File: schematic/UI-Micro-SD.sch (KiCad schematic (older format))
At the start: 31 parts, among them IC1 TCA9534PWR, J1 Conn_02x08_Odd_Even, J2 Conn_02x08_Odd_Even, J6 Conn_01x08, J8 Solder-Jumper-3-3-3-Open, Q1 BSS138, U1 SFV14R-2STE1HLF, U2 DizzyBITLogo, U3 DizzyBIT-Layout

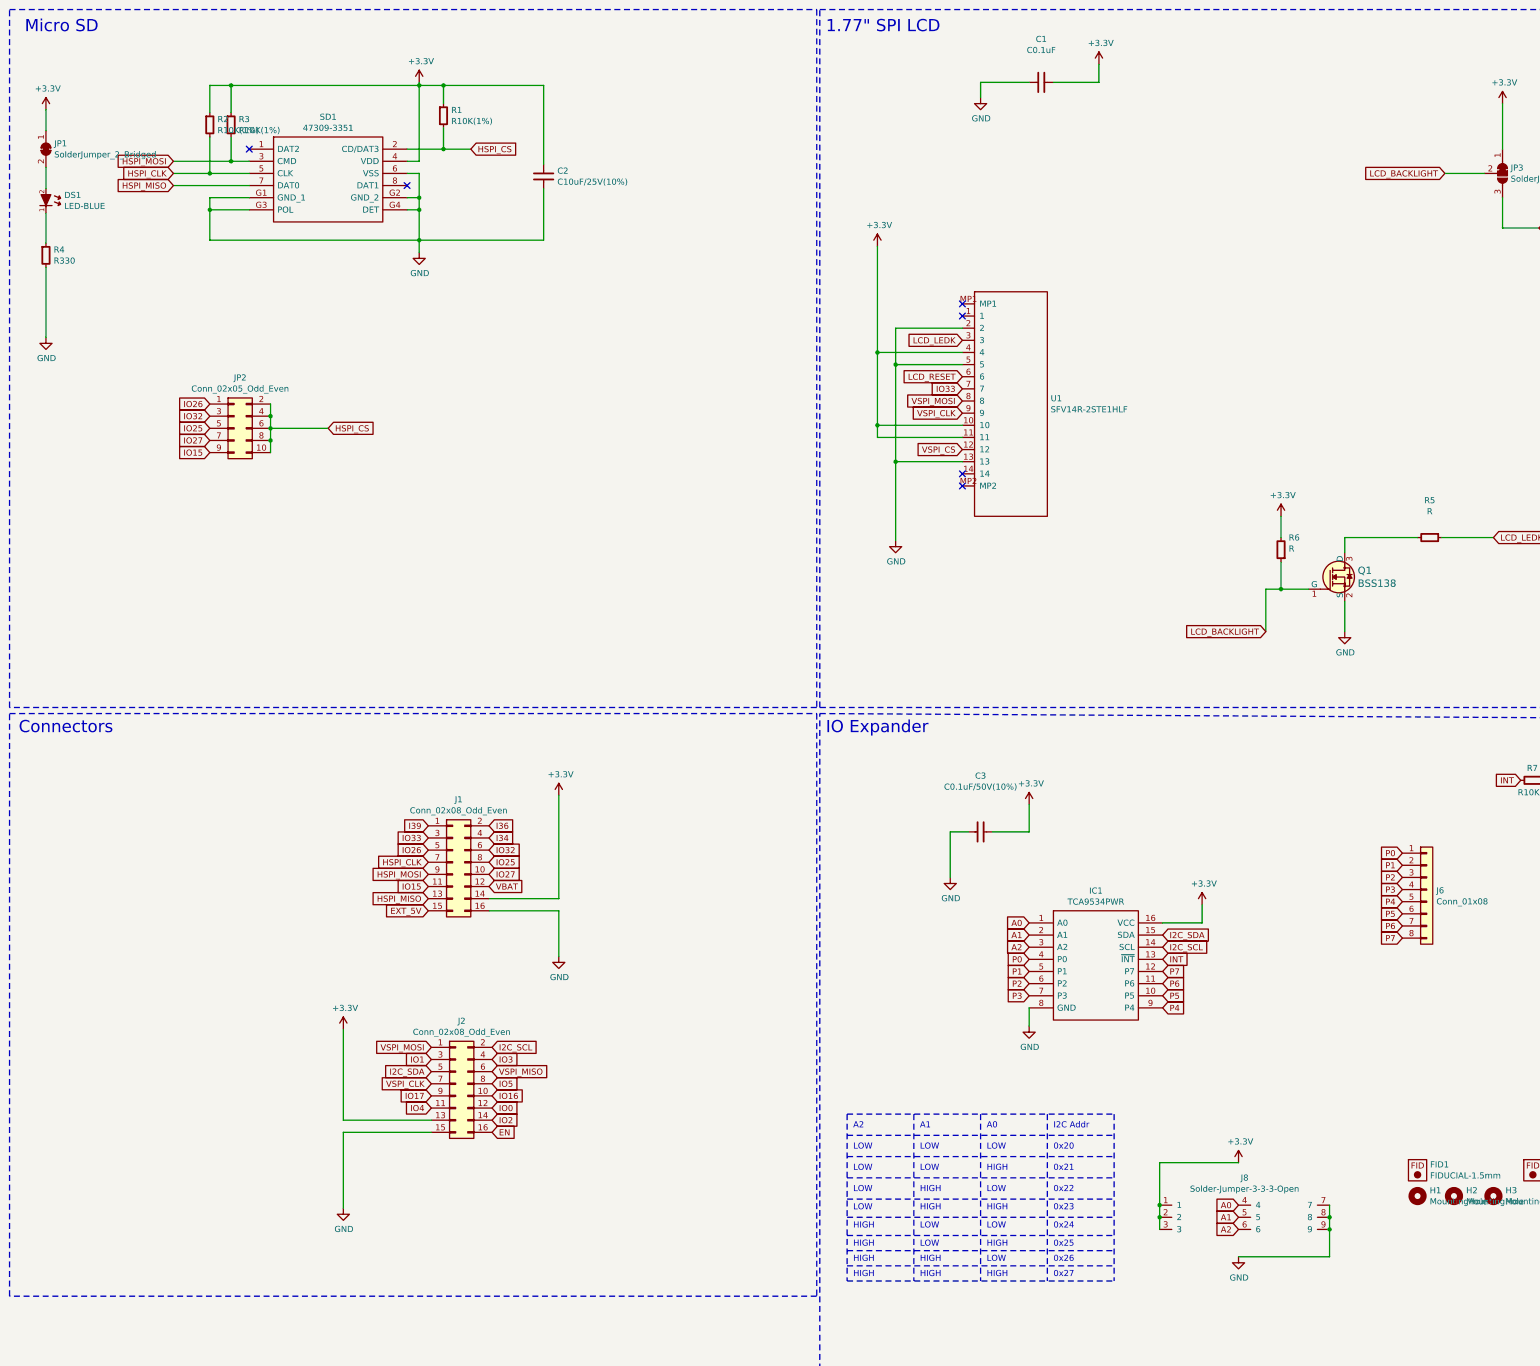
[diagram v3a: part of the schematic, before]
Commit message: Fixed PN-s for display connector and IO expander
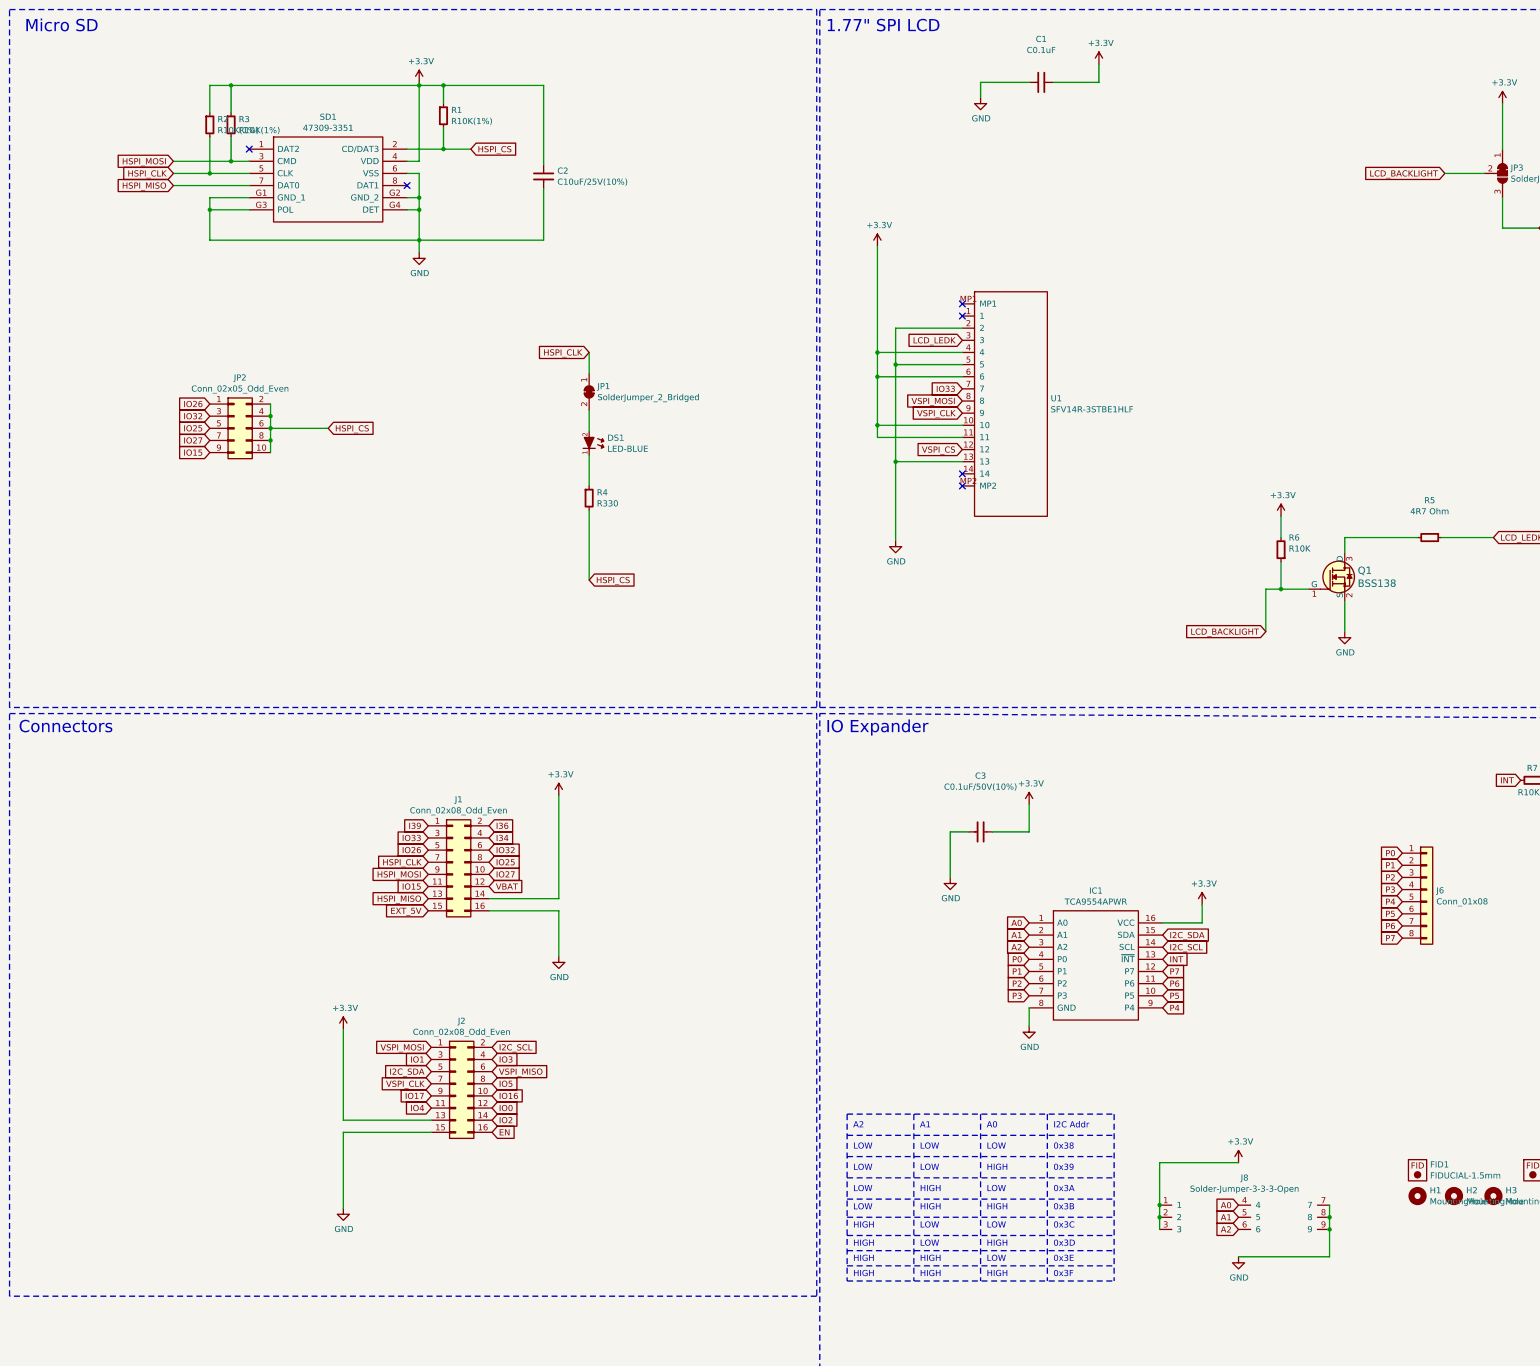
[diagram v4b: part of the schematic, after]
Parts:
- removed IC1: TCA9534PWR, undo:SOP65P640X120-16N, symbol SamacSys_Parts:TCA9534PWR
- added IC1: TCA9554APWR, SOP65P640X120-16N, symbol SamacSys_Parts:TCA9554APWR
- R5: value R -> 4R7 Ohm; pn (none) -> RC0603JR-074R7L
- R6: value R -> R10K; pn ESR03EZPJ103 -> ESR03EZPJ103
- SD1: Description Molex 47309 Series 8 Way Right Angle Micro SD Memory Card C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 -> (none); Height 3.35 -> (none); Manufacturer_Name Molex -> Connfly; Manufacturer_Part_Number 47309-3351 -> DS1139-05; Mouser Part Number 538-47309-3351 -> (none); dk_pn WM10795DKR-ND -> (none); pn 47309-3351 -> DS1139-05
- U1: value SFV14R-2STE1HLF -> SFV14R-3STBE1HLF; footprint undo:SFV14R-2STE1HLF -> undo:SFV14R-3STBE1HLF
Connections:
- net LCD_RESET is gone; now on net +3V3: U1.6
- net +3V3: now also IC1.16 (VCC); no longer JP1.1 (A)
- net A0: now also IC1.1 (A0)
- net A1: now also IC1.2 (A1)
- net A2: now also IC1.3 (A2)
- net GND: now also IC1.8 (GND); no longer R4.2
- net HSPI_CLK: now also JP1.1 (A)
- net HSPI_CS: now also R4.2
- net I2C_SCL: now also IC1.14 (SCL)
- net I2C_SDA: now also IC1.15 (SDA)
- net INT: now also IC1.13 (~INT)
- net P0: now also IC1.4 (P0)
- net P1: now also IC1.5 (P1)
- net P2: now also IC1.6 (P2)
- net P3: now also IC1.7 (P3)
- net P4: now also IC1.9 (P4)
- net P5: now also IC1.10 (P5)
- net P6: now also IC1.11 (P6)
- net P7: now also IC1.12 (P7)
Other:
- note added: "0x38"
- note added: "0x39"
- note added: "0x3A"
- note added: "0x3B"
- note added: "0x3C"
- note added: "0x3D"
- note added: "0x3E"
- note added: "0x3F\n"
- note removed: "0x20"
- note removed: "0x21"
- note removed: "0x22"
- note removed: "0x23"
- note removed: "0x24"
- note removed: "0x25"
- note removed: "0x26"
- note removed: "0x27\n"
- moved on the sheet: DS1, JP1, R4
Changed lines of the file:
@@
 L _semi:LED DS1
 U 1 1 5C6120FB
-P 875 2150
-F 0 "DS1" H 1025 2196 50  0000 L CNN
-F 1 "LED-BLUE" H 1025 2105 50  0000 L CNN
-F 2 "LED_SMD:LED_0805_2012Metric" H 1025 2104 60  0001 L CNN
-F 3 "" H 875 2150 60  0001 C CNN
-F 4 "160-1579-1-ND" H 1025 2006 50  0001 L CNN "dk_pn"
-F 5 "LTST-C170TBKT" H 875 2150 50  0001 C CNN "pn"
-F 6 "https://www.digikey.com/product-detail/en/lite-on-inc/LTST-C170TBKT/160-1579-1-ND/564889" H 875 2150 50  0001 C CNN "dk_web"
-	1    875  2150
+P 5350 4150
+F 0 "DS1" H 5500 4196 50  0000 L CNN
+F 1 "LED-BLUE" H 5500 4105 50  0000 L CNN
+F 2 "LED_SMD:LED_0805_2012Metric" H 5500 4104 60  0001 L CNN
+F 3 "" H 5350 4150 60  0001 C CNN
+F 4 "160-1579-1-ND" H 5500 4006 50  0001 L CNN "dk_pn"
+F 5 "LTST-C170TBKT" H 5350 4150 50  0001 C CNN "pn"
+F 6 "https://www.digikey.com/product-detail/en/lite-on-inc/LTST-C170TBKT/160-1579-1-ND/564889" H 5350 4150 50  0001 C CNN "dk_web"
+	1    5350 4150
 	1    0    0    -1
 $EndComp
@@
 L _passive:R R4
 U 1 1 5C61218D
-P 875 2600
-F 0 "R4" H 938 2646 50  0000 L CNN
-F 1 "R330" H 938 2555 50  0000 L CNN
-F 2 "Resistor_SMD:R_0603_1608Metric" H 875 2650 60  0001 C CNN
-F 3 "" H 875 2650 60  0001 C CNN
-F 4 "CR0603-JW-331ELFCT-ND" H 875 2600 50  0001 C CNN "dk_pn"
-F 5 "CR0603-JW-331ELF" H 875 2600 50  0001 C CNN "pn"
-F 6 "https://www.digikey.com/product-detail/en/bourns-inc/CR0603-JW-331ELF/CR0603-JW-331ELFCT-ND/3767680" H 875 2600 50  0001 C CNN "dk_web"
-	1    875  2600
-	1    0    0    -1
-$EndComp
-$Comp
-L power:+3.3V #PWR0101
-U 1 1 5C6121E5
-P 875 1400
-F 0 "#PWR0101" H 875 1250 50  0001 C CNN
-F 1 "+3.3V" H 890 1573 50  0000 C CNN
-F 2 "" H 875 1400 50  0001 C CNN
-F 3 "" H 875 1400 50  0001 C CNN
-	1    875  1400
-	1    0    0    -1
-$EndComp
-Wire Wire Line
-	875  2050 875  1875
-$Comp
-L power:GND #PWR0102
-U 1 1 5C612F06
-P 875 3275
-F 0 "#PWR0102" H 875 3025 50  0001 C CNN
-F 1 "GND" H 880 3102 50  0000 C CNN
-F 2 "" H 875 3275 50  0001 C CNN
-F 3 "" H 875 3275 50  0001 C CNN
-	1    875  3275
-	1    0    0    -1
-$EndComp
-Wire Wire Line
-	875  2700 875  3275
-Wire Wire Line
-	875  2250 875  2500
+P 5350 4600
+F 0 "R4" H 5413 4646 50  0000 L CNN
+F 1 "R330" H 5413 4555 50  0000 L CNN
+F 2 "Resistor_SMD:R_0603_1608Metric" H 5350 4650 60  0001 C CNN
+F 3 "" H 5350 4650 60  0001 C CNN
+F 4 "CR0603-JW-331ELFCT-ND" H 5350 4600 50  0001 C CNN "dk_pn"
+F 5 "CR0603-JW-331ELF" H 5350 4600 50  0001 C CNN "pn"
+F 6 "https://www.digikey.com/product-detail/en/bourns-inc/CR0603-JW-331ELF/CR0603-JW-331ELFCT-ND/3767680" H 5350 4600 50  0001 C CNN "dk_web"
+	1    5350 4600
+	1    0    0    -1
+$EndComp
+Wire Wire Line
+	5350 4050 5350 3875
+Wire Wire Line
+	5350 4700 5350 5275
+Wire Wire Line
+	5350 4250 5350 4500
 $Comp
 L SamacSys_Parts:47309-3351 SD1
@@
 F 2 "Connfly:DS1139-05" H 3700 1825 50  0001 L CNN
 F 3 "https://componentsearchengine.com/Datasheets/1/47309-3351.pdf" H 3700 1725 50  0001 L CNN
-F 4 "WM10795DKR-ND" H 2550 1725 50  0001 C CNN "dk_pn"
-F 5 "47309-3351" H 2550 1725 50  0001 C CNN "pn"
-F 6 "Molex 47309 Series 8 Way Right Angle Micro SD Memory Card Connector with Solder Termination" H 3700 1625 50  0001 L CNN "Description"
-F 7 "3.35" H 3700 1525 50  0001 L CNN "Height"
-F 8 "538-47309-3351" H 3700 1425 50  0001 L CNN "Mouser Part Number"
-F 9 "Molex" H 3700 1325 50  0001 L CNN "Manufacturer_Name"
-F 10 "47309-3351" H 3700 1225 50  0001 L CNN "Manufacturer_Part_Number"
+F 4 "DS1139-05" H 2550 1725 50  0001 C CNN "pn"
+F 5 "Connfly" H 3700 1325 50  0001 L CNN "Manufacturer_Name"
+F 6 "DS1139-05" H 3700 1225 50  0001 L CNN "Manufacturer_Part_Number"
 	1    2550 1725
 	1    0    0    -1
@@
 P 8525 2850
 F 0 "U1" H 9152 1921 50  0000 L CNN
-F 1 "SFV14R-2STE1HLF" H 9152 1830 50  0000 L CNN
-F 2 "undo:SFV14R-2STE1HLF" H 8525 2850 50  0001 C CNN
+F 1 "SFV14R-3STBE1HLF" H 9152 1830 50  0000 L CNN
+F 2 "undo:SFV14R-3STBE1HLF" H 8525 2850 50  0001 C CNN
 F 3 "" H 8525 2850 50  0001 C CNN
 	1    8525 2850
@@
 Text GLabel 8425 3300 0    50   Input ~ 0
 LCD_LEDK
-Text GLabel 8425 3600 0    50   Input ~ 0
-LCD_RESET
 $Comp
 L OLIMEX_Power:+3.3V #PWR0110
@@
 Connection ~ 7725 3400
 Wire Wire Line
-	7725 3400 7725 4000
+	7725 3400 7725 3600
 $Comp
 L dk_Transistors-FETs-MOSFETs-Single:BSS138 Q1
@@
 P 12275 4925
 F 0 "R5" V 11969 4925 50  0000 C CNN
-F 1 "R" V 12060 4925 50  0000 C CNN
+F 1 "4R7 Ohm" V 12060 4925 50  0000 C CNN
 F 2 "Resistor_SMD:R_0603_1608Metric" V 12159 4925 60  0001 C CNN
 F 3 "" H 12275 4975 60  0000 C CNN
+F 4 "RC0603JR-074R7L " H 12275 4925 50  0001 C CNN "pn"
 	1    12275 4925
 	0    1    1    0
@@
 P 11050 5025
 F 0 "R6" H 10987 4926 50  0000 R CNN
-F 1 "R" H 10987 5017 50  0000 R CNN
+F 1 "R10K" H 10987 5017 50  0000 R CNN
 F 2 "Resistor_SMD:R_0603_1608Metric" H 10987 5116 60  0001 R CNN
 F 3 "" H 11050 5075 60  0000 C CNN
-F 4 "ESR03EZPJ103" H 11050 5025 50  0001 C CNN "pn"
+F 4 "ESR03EZPJ103 " H 11050 5025 50  0001 C CNN "pn"
 	1    11050 5025
 	-1   0    0    1
@@
 Text Notes 7300 775  0    100  ~ 0
 1.77" SPI LCD
-$Comp
-L SamacSys_Parts:TCA9534PWR IC1
-U 1 1 5C5946A2
-P 8975 8100
-F 0 "IC1" H 9525 8365 50  0000 C CNN
-F 1 "TCA9534PWR" H 9525 8274 50  0000 C CNN
-F 2 "undo:SOP65P640X120-16N" H 9925 8200 50  0001 L CNN
-F 3 "http://www.ti.com/lit/ds/symlink/tca9534.pdf" H 9925 8100 50  0001 L CNN
-F 4 "296-40574-1-ND" H 8975 8100 50  0001 C CNN "dk_pn"
-F 5 "TCA9534PWR" H 8975 8100 50  0001 C CNN "pn"
-F 6 "Remote 8-Bit I2C Low-Power I/O Expander With Interrupt Output and Configuration Registers" H 9925 8000 50  0001 L CNN "Description"
-F 7 "1.2" H 9925 7900 50  0001 L CNN "Height"
-F 8 "595-TCA9534PWR" H 9925 7800 50  0001 L CNN "Mouser Part Number"
-F 9 "Texas Instruments" H 9925 7700 50  0001 L CNN "Manufacturer_Name"
-F 10 "TCA9534PWR" H 9925 7600 50  0001 L CNN "Manufacturer_Part_Number"
-	1    8975 8100
-	1    0    0    -1
-$EndComp
 $Comp
 L power:+3.3V #PWR0116
@@
 LOW
 Text Notes 9175 9975 0    50   ~ 0
-0x20
+0x38
 Wire Notes Line
 	7475 10025 9675 10025
@@
 HIGH
 Text Notes 9175 10150 0    50   ~ 0
-0x21
+0x39
 Wire Notes Line
 	7475 10200 9675 10200
@@
 LOW
 Text Notes 9175 10325 0    50   ~ 0
-0x22
+0x3A
 Wire Notes Line
 	7475 10375 9675 10375
@@
 HIGH
 Text Notes 9175 10475 0    50   ~ 0
-0x23
+0x3B
 Wire Notes Line
 	7475 10525 9675 10525
@@
 LOW
 Text Notes 9175 10625 0    50   ~ 0
-0x24
+0x3C
 Wire Notes Line
 	7475 10675 9675 10675
@@
 HIGH
 Text Notes 9175 10775 0    50   ~ 0
-0x25
+0x3D
 Wire Notes Line
 	7475 10800 9675 10800
@@
 LOW
 Text Notes 9175 10900 0    50   ~ 0
-0x26
+0x3E
 Wire Notes Line
 	7475 10925 9675 10925
@@
 HIGH
 Text Notes 9175 11025 0    50   ~ 0
-0x27\n
+0x3F\n
 Wire Notes Line
 	7475 11050 9675 11050
@@
 L Jumper:SolderJumper_2_Bridged JP1
 U 1 1 5D97861B
-P 875 1725
-F 0 "JP1" V 829 1793 50  0000 L CNN
-F 1 "SolderJumper_2_Bridged" V 920 1793 50  0000 L CNN
-F 2 "DizzyBit:DizzyBit-SolderJumper-2-Open" H 875 1725 50  0001 C CNN
-F 3 "~" H 875 1725 50  0001 C CNN
-	1    875  1725
+P 5350 3725
+F 0 "JP1" V 5304 3793 50  0000 L CNN
+F 1 "SolderJumper_2_Bridged" V 5395 3793 50  0000 L CNN
+F 2 "DizzyBit:DizzyBit-SolderJumper-2-Open" H 5350 3725 50  0001 C CNN
+F 3 "~" H 5350 3725 50  0001 C CNN
+	1    5350 3725
 	0    1    1    0
 $EndComp
 Wire Wire Line
-	875  1400 875  1575
+	5350 3400 5350 3575
 NoConn ~ 8425 3000
 Wire Wire Line
@@
 Wire Wire Line
 	10050 10525 10050 10625
+Wire Wire Line
+	8425 3600 7725 3600
+Connection ~ 7725 3600
+Wire Wire Line
+	7725 3600 7725 4000
+Text GLabel 5350 3400 0    50   Input ~ 0
+HSPI_CLK
+Text GLabel 5350 5275 2    50   Input ~ 0
+HSPI_CS
+$Comp
+L SamacSys_Parts:TCA9554APWR IC1
+U 1 1 5DBD5E3F
+P 8975 8100
+F 0 "IC1" H 9525 8365 50  0000 C CNN
+F 1 "TCA9554APWR" H 9525 8274 50  0000 C CNN
+F 2 "SOP65P640X120-16N" H 9925 8200 50  0001 L CNN
+F 3 "http://www.ti.com/lit/gpn/tca9554a" H 9925 8100 50  0001 L CNN
+F 4 "Texas Instruments TCA9554APWR, 8-channel 8bit I/O Expander 400kHz, I2C, SMBus, 16-Pin TSSOP" H 9925 8000 50  0001 L CNN "Description"
+F 5 "" H 9925 7900 50  0001 L CNN "Height"
+F 6 "595-TCA9554APWR" H 9925 7800 50  0001 L CNN "Mouser Part Number"
+F 7 "https://www.mouser.com/Search/ProductDetail.aspx?qs=O1HRStiETCjcEMAC%252bg%252bJsA%3d%3d" H 9925 7700 50  0001 L CNN "Mouser Price/Stock"
+F 8 "Texas Instruments" H 9925 7600 50  0001 L CNN "Manufacturer_Name"
+F 9 "TCA9554APWR" H 9925 7500 50  0001 L CNN "Manufacturer_Part_Number"
+	1    8975 8100
+	1    0    0    -1
+$EndComp
 $EndSCHEMATC
